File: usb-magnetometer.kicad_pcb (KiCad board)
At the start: 4 copper layers, 88.8 x 19.8 mm, 43 parts, among them J1 USB_C_Receptacle_USB2.0, J2 1x5_MALE, J3 1x2_Male, U1 FT231XS, U2 TMAG5170, U3 STM32L010C6T6

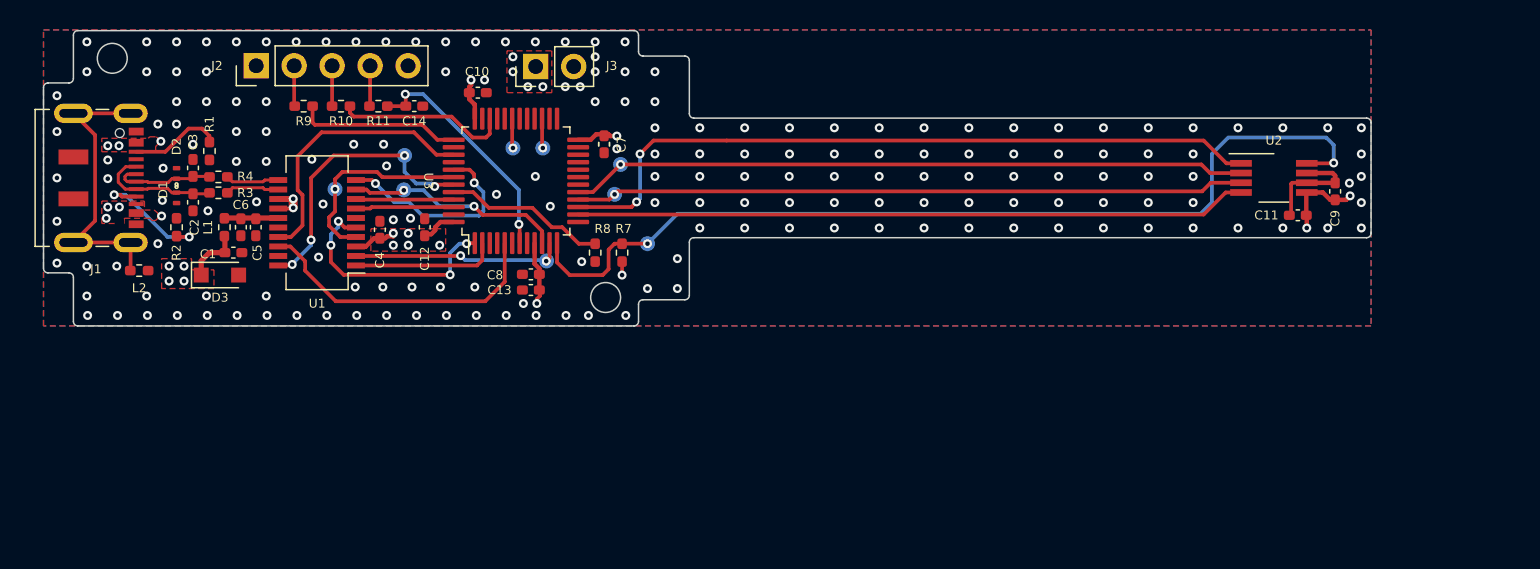
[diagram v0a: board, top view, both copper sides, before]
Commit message: Add initial version of separated pcbs
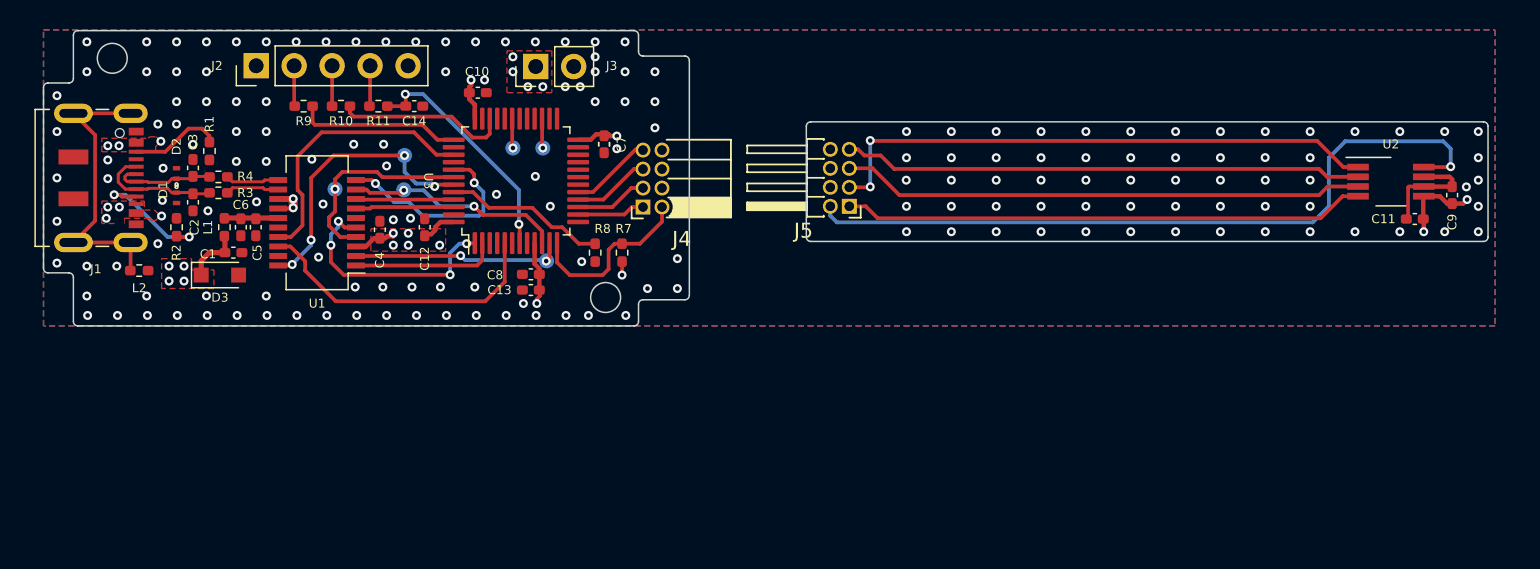
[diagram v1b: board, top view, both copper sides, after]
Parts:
- removed TP3, TP4, TP5: TestPoint_Small, TestPoint:TestPoint_Pad_D1.0mm
- added J4: Conn_02x04_Odd_Even, Connector_PinSocket_1.27mm:PinSocket_2x04_P1.27mm_Horizontal, F.Cu at (88.2, 145.1)
- added J5: Conn_02x04_Odd_Even, Connector_PinHeader_1.27mm:PinHeader_2x04_P1.27mm_Horizontal, F.Cu at (102.0, 145.0)
- moved C11 7.83 mm to (139.8, 145.8)
- moved C9 7.83 mm to (142.3, 144.2)
- moved U2 7.83 mm to (138.2, 143.3)
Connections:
- U2 pad 1: /SPI_SCK -> /SPI_SCK_S
- U2 pad 2: /SPI_MOSI -> /SPI_MOSI_S
- U2 pad 3: /SPI_MISO -> /SPI_MISO_S
- U2 pad 4: /SPI_NSS -> /SPI_NSS_S
- U2 pad 8: /MAG_INT -> /MAG_INT_S
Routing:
- net /MAG_INT: track 63.3 -> 11.9 mm, vias 2 -> 0
- net /MAG_INT_S: track 0.00 -> 49.7 mm, vias 0 -> 1
- net /SPI_SCK: track 48.6 -> 4.86 mm, vias 2 -> 0
- net /SPI_NSS: track 44.9 -> 4.54 mm
- net /SPI_MOSI: track 45.3 -> 5.53 mm, vias 1 -> 0
- net /SPI_MISO: track 44.8 -> 5.18 mm, vias 1 -> 0
- net /SPI_SCK_S: track 0.00 -> 37.9 mm, vias 0 -> 2
- net /SPI_MISO_S: track 0.00 -> 35.0 mm
- net /SPI_NSS_S: track 0.00 -> 35.0 mm
- net /SPI_MOSI_S: track 0.00 -> 34.8 mm
- net GND: vias 179 -> 166
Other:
- board size 88.8 x 19.8 mm -> 96.6 x 19.8 mm

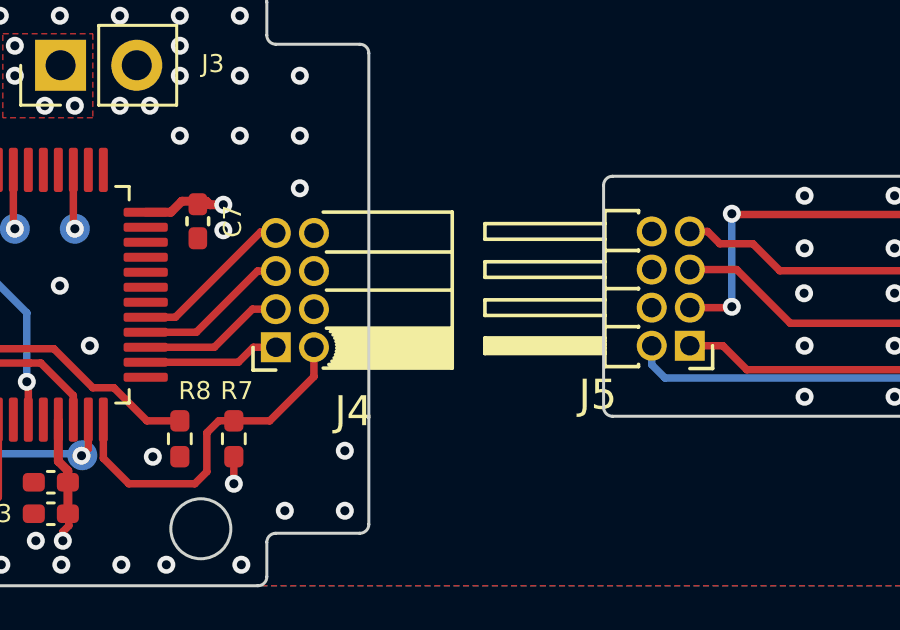
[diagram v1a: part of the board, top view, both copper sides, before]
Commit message: Update conenctors designators size
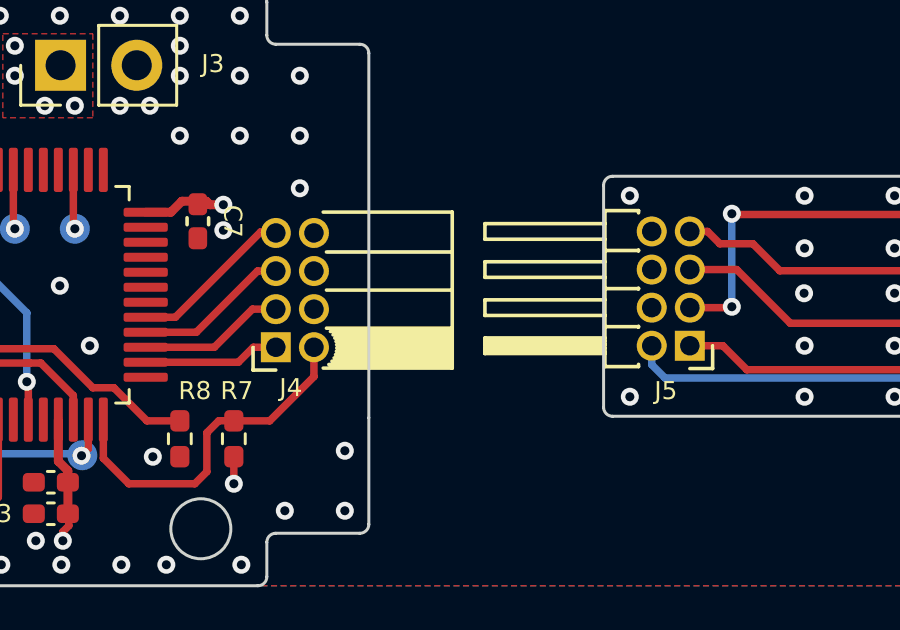
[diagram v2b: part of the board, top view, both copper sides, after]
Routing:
- net GND: vias 166 -> 168
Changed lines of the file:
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@@
     (property "Sheetname" "")
     (attr through_hole)
-    (fp_text reference "J4" (at -2.5925 -2.135) (layer "F.SilkS")
-      (effects (font (size 1 1) (thickness 0.15)))
+    (fp_text reference "J4" (at -0.5 -1.35 unlocked) (layer "F.SilkS")
+      (effects (font (size 0.6 0.6) (thickness 0.1)))
     )
     (fp_text value "Conn_02x04_Odd_Even" (at -2.5925 5.945) (layer "F.Fab")
       (effects (font (size 1 1) (thickness 0.15)))
     )
-    (fp_text user "${REFERENCE}" (at -3.62 1.905 90) (layer "F.Fab")
+    (fp_text user "${REFERENCE}" (at -3.62 1.905 90 unlocked) (layer "F.Fab")
       (effects (font (size 1 1) (thickness 0.15)))
     )
@@
       (effects (font (size 1 1) (thickness 0.15)))
     )
-    (fp_text user "${REFERENCE}" (at 0 5.08 180) (layer "F.Fab")
+    (fp_text user "${REFERENCE}" (at 0 5.08 180 unlocked) (layer "F.Fab")
       (effects (font (size 1 1) (thickness 0.15)))
     )
@@
     (property "Sheetname" "")
     (attr through_hole)
-    (fp_text reference "J5" (at 3.0675 -1.635) (layer "F.SilkS")
-      (effects (font (size 1 1) (thickness 0.15)))
+    (fp_text reference "J5" (at 0.8 -1.5 unlocked) (layer "F.SilkS")
+      (effects (font (size 0.6 0.6) (thickness 0.1)))
     )
     (fp_text value "Conn_02x04_Odd_Even" (at 3.0675 5.445) (layer "F.Fab")
       (effects (font (size 1 1) (thickness 0.15)))
     )
-    (fp_text user "${REFERENCE}" (at 2.27 1.905 90) (layer "F.Fab")
-      (effects (font (size 0.6 0.6) (thickness 0.09)))
+    (fp_text user "${REFERENCE}" (at 2.27 1.905 90 unlocked) (layer "F.Fab")
+      (effects (font (size 1 1) (thickness 0.15)))
     )
     (fp_line (start -0.76 0) (end -0.76 -0.76) (layer "F.SilkS") (width 0.12))
@@
     (property "Sheetname" "")
     (attr smd)
-    (fp_text reference "C7" (at 0 -1.16 -90) (layer "F.SilkS")
+    (fp_text reference "C7" (at 0 -1.16 -90 unlocked) (layer "F.SilkS")
       (effects (font (size 0.6 0.6) (thickness 0.1)))
     )
@@
       (effects (font (size 1 1) (thickness 0.15)))
     )
-    (fp_text user "${REFERENCE}" (at 0 0 -90) (layer "F.Fab")
+    (fp_text user "${REFERENCE}" (at 0 0 -90 unlocked) (layer "F.Fab")
       (effects (font (size 1 1) (thickness 0.15)))
     )
@@
   (via (at 144.075 145) (size 0.6) (drill 0.3) (layers "F.Cu" "B.Cu") (free) (net 1))
   (via (at 84 137) (size 0.6) (drill 0.3) (layers "F.Cu" "B.Cu") (free) (net 1))
+  (via (at 100 140) (size 0.6) (drill 0.3) (layers "F.Cu" "B.Cu") (free) (net 1))
   (via (at 66.5 148.4) (size 0.6) (drill 0.3) (layers "F.Cu" "B.Cu") (free) (net 1))
   (via (at 49 137.6) (size 0.6) (drill 0.3) (layers "F.Cu" "B.Cu") (free) (net 1))
@@
   (via (at 126.825 143.25) (size 0.6) (drill 0.3) (layers "F.Cu" "B.Cu") (free) (net 1))
   (via (at 63.05 152.3) (size 0.6) (drill 0.3) (layers "F.Cu" "B.Cu") (free) (net 1))
+  (via (at 100 146.7) (size 0.6) (drill 0.3) (layers "F.Cu" "B.Cu") (free) (net 1))
   (via (at 67.05 152.3) (size 0.6) (drill 0.3) (layers "F.Cu" "B.Cu") (free) (net 1))
   (via (at 114.825 146.7) (size 0.6) (drill 0.3) (layers "F.Cu" "B.Cu") (free) (net 1))

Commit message: FPC connectors in progress
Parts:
- added J6: Conn_02x04_Odd_Even, Connector_PinHeader_1.00mm:PinHeader_2x04_P1.00mm_Vertical, F.Cu at (131.9, 165.9)
- added J7: Conn_02x04_Odd_Even, Connector_PinHeader_1.00mm:PinHeader_2x04_P1.00mm_Vertical, F.Cu at (91.4, 141.8)
- J4: footprint Connector_PinSocket_1.27mm:PinSocket_2x04_P1.27mm_Horizontal -> Connector_FFC-FPC:Hirose_FH12-8S-0.5SH_1x08-1MP_P0.50mm_Horizontal; moved to B.Cu
- J5: footprint Connector_PinHeader_1.27mm:PinHeader_2x04_P1.27mm_Horizontal -> Connector_FFC-FPC:Hirose_FH12-8S-0.5SH_1x08-1MP_P0.50mm_Horizontal; moved to B.Cu
- moved J4 49.8 mm to (135.4, 160.9)
- moved U2 18.8 mm to (135.4, 161.9)
- moved C9 18.6 mm to (139.3, 162.6)
- moved C11 18.6 mm to (137.0, 164.2)
- moved J5 12.8 mm to (89.3, 143.3), turned to -90 degrees
- moved C7 1.66 mm to (85.8, 139.2), turned to 0 degrees
- moved R7 1.28 mm to (87.6, 147.1), turned to 90 degrees
- moved C1 1.00 mm to (61.8, 148.1)
- moved C10 1.00 mm to (78.2, 137.4)
- moved C12 1.00 mm to (74.6, 146.4)
- moved C13 1.00 mm to (81.7, 150.6)
- moved C14 1.00 mm to (73.9, 138.3)
- moved C2 1.00 mm to (59.1, 144.7)
- moved C3 1.00 mm to (59.1, 142.4)
- moved C4 1.00 mm to (71.6, 146.6)
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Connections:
- C11 pad 1: VDD -> /VDD_S
- C11 pad 2: GND -> /GND_S
- C9 pad 1: VDD -> /VDD_S
- C9 pad 2: GND -> /GND_S
- J4 pad 1: /SPI_NSS -> /MAG_INT_S
- J4 pad 2: /MAG_INT -> /VDD_S
- J4 pad 3: /SPI_SCK -> /SPI_NSS_S
- J4 pad 4: GND -> /GND_S
- J4 pad 5: /SPI_MISO -> /SPI_MISO_S
- J4 pad 6: GND -> /SPI_MOSI_S
- J4 pad 7: /SPI_MOSI -> /GND_S
- J4 pad 8: VDD -> /SPI_SCK_S
- J5 pad 1: /SPI_NSS_S -> /SPI_SCK
- J5 pad 2: /MAG_INT_S -> GND
- J5 pad 3: /SPI_SCK_S -> /SPI_MOSI
- J5 pad 4: GND -> /SPI_MISO
- J5 pad 5: /SPI_MISO_S -> GND
- J5 pad 6: GND -> /SPI_NSS
- J5 pad 7: /SPI_MOSI_S -> VDD
- J5 pad 8: VDD -> /MAG_INT
- U2 pad 5: VDD -> /VDD_S
- U2 pad 6: GND -> /GND_S
- U2 pad 7: GND -> /GND_S
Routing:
- net /MAG_INT_S: track 49.7 -> 7.90 mm
- net /SPI_SCK_S: track 37.9 -> 7.00 mm, vias 2 -> 1
- net /SPI_MOSI_S: track 34.8 -> 12.3 mm, vias 0 -> 1
- net /SPI_MISO_S: track 35.0 -> 14.2 mm, vias 0 -> 1
- net /SPI_NSS_S: track 35.0 -> 17.9 mm, vias 0 -> 1
- net /MAG_INT: track 11.9 -> 25.3 mm, vias 0 -> 1
- net /SPI_MISO: track 5.18 -> 13.3 mm, vias 0 -> 1
- net GND: track 7.59 -> 0.03 mm, vias 168 -> 100
- net /SPI_SCK: track 4.86 -> 11.6 mm, vias 0 -> 2
- net /SPI_NSS: track 4.54 -> 10.9 mm, vias 0 -> 1
- net VDD: track 24.2 -> 17.9 mm
- net /GND_S: track 0.00 -> 5.83 mm, vias 0 -> 1
- net /VDD_S: track 0.00 -> 5.21 mm, vias 0 -> 1
- net /SPI_MOSI: track 5.53 -> 9.86 mm, vias 0 -> 1
- net Net-(J1-PadB5): track 8.59 -> 5.18 mm, vias 2 -> 0
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- added copper zone on B.Cu, net VDD
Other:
- board size 96.6 x 19.8 mm -> 92.6 x 33.9 mm

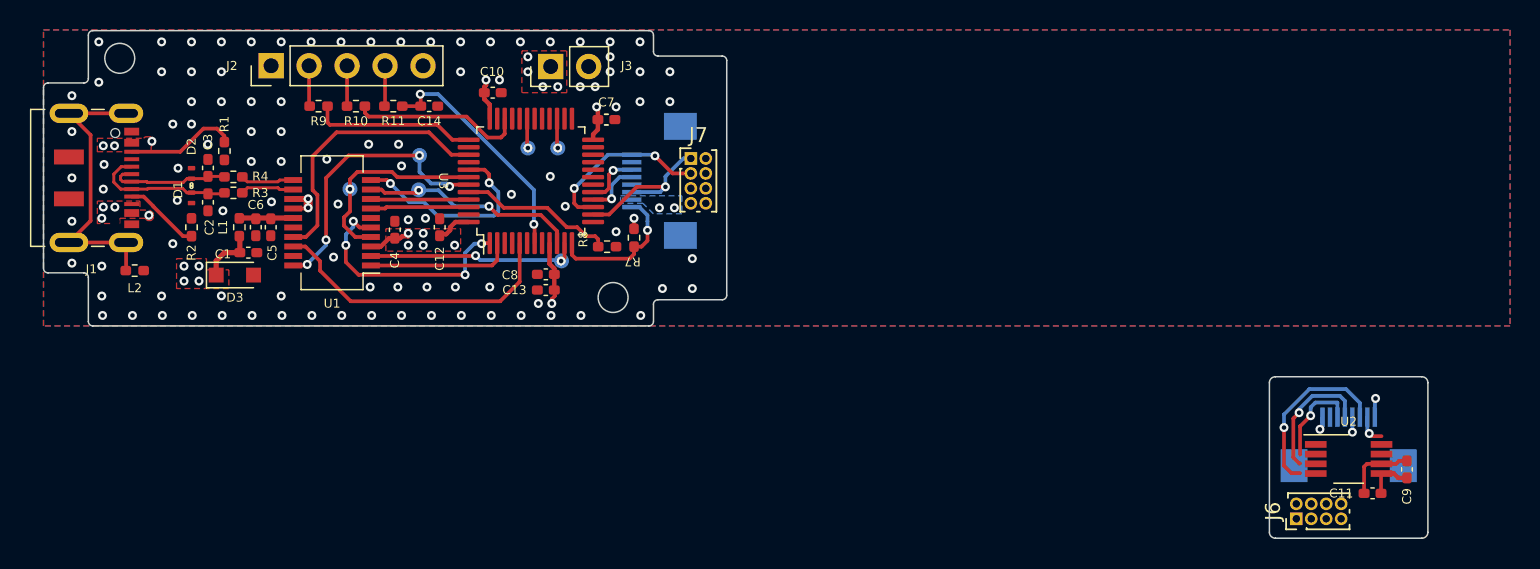
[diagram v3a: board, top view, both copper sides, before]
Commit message: Add final version with sensor on separated pcb
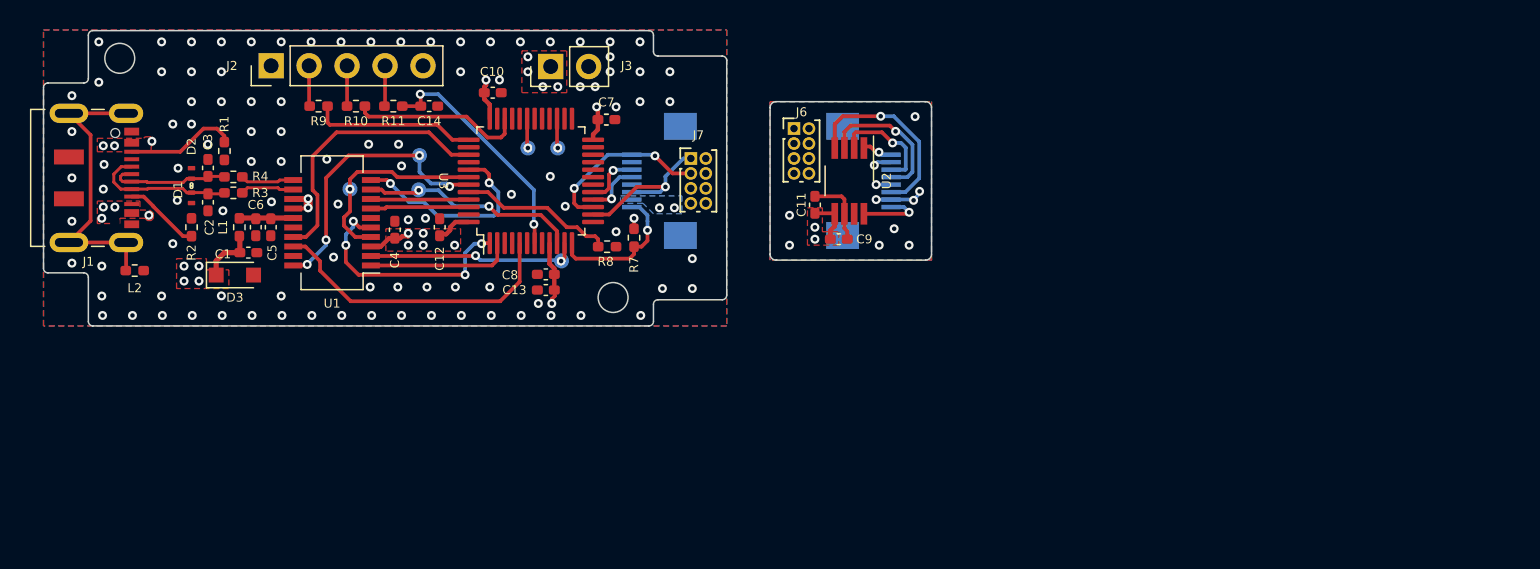
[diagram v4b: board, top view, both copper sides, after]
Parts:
- moved J6 42.5 mm to (98.3, 139.8), turned to 0 degrees
- moved C11 42.0 mm to (99.7, 144.9), turned to 90 degrees
- moved C9 41.0 mm to (101.3, 147.2), turned to 0 degrees
- moved U2 38.2 mm to (102.0, 143.3), turned to -90 degrees
- moved J4 36.9 mm to (103.0, 143.3), turned to 90 degrees
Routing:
- net /MAG_INT_S: track 7.90 -> 13.3 mm
- net /SPI_MISO_S: track 14.2 -> 15.8 mm
- net /SPI_NSS_S: track 17.9 -> 19.4 mm
- net /VDD_S: track 5.21 -> 6.51 mm, vias 1 -> 5
- net /GND_S: track 5.83 -> 7.03 mm, vias 1 -> 8
- net /SPI_MOSI_S: track 12.3 -> 13.3 mm
- net /SPI_SCK_S: track 7.00 -> 7.79 mm
- added copper zone on B.Cu, net /GND_S
- added copper zone on F.Cu, net /GND_S
- added copper zone on In1.Cu, net /GND_S
- added copper zone on F.Cu, net /VDD_S
- added copper zone on In2.Cu, net /VDD_S
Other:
- board size 92.6 x 33.9 mm -> 59.4 x 19.8 mm
